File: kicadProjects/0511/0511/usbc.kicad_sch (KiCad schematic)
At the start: 13 parts, among them J1 USB4120-03-C_REVA6, U7 BD33HC5WEFJ-E2

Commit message: started to annotate and place buttons on pcb
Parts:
- renumbered CR2 to CR1, R154 to R151, R155 to R152, R156 to R153
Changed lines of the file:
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@@
 		(dnp no)
 		(fields_autoplaced yes)
-		(property "Reference" "#PWR0198"
+		(property "Reference" "#PWR0195"
 			(at 46.99 53.34 0)
 			(effects
@@
 			(project "0511"
 				(path "/2c0b0e0d-c5e7-48b7-93bb-9be1941509af/7f025c79-ea20-4013-a71e-871359ae3c80/be8e2f48-706b-43bd-b6e8-a7bcf8b61384"
-					(reference "#PWR0198")
+					(reference "#PWR0195")
 					(unit 1)
 				)
@@
 		(dnp no)
 		(fields_autoplaced yes)
-		(property "Reference" "#PWR0203"
+		(property "Reference" "#PWR0200"
 			(at 90.17 134.62 0)
 			(effects
@@
 			(project "0511"
 				(path "/2c0b0e0d-c5e7-48b7-93bb-9be1941509af/7f025c79-ea20-4013-a71e-871359ae3c80/be8e2f48-706b-43bd-b6e8-a7bcf8b61384"
-					(reference "#PWR0203")
+					(reference "#PWR0200")
 					(unit 1)
 				)
@@
 		(dnp no)
 		(fields_autoplaced yes)
-		(property "Reference" "#PWR0195"
+		(property "Reference" "#PWR0192"
 			(at 121.92 39.37 0)
 			(effects
@@
 			(project "0511"
 				(path "/2c0b0e0d-c5e7-48b7-93bb-9be1941509af/7f025c79-ea20-4013-a71e-871359ae3c80/be8e2f48-706b-43bd-b6e8-a7bcf8b61384"
-					(reference "#PWR0195")
+					(reference "#PWR0192")
 					(unit 1)
 				)
@@
 		(dnp no)
 		(fields_autoplaced yes)
-		(property "Reference" "R155"
+		(property "Reference" "R152"
 			(at 87.63 119.3799 0)
 			(effects
@@
 			(project "0511"
 				(path "/2c0b0e0d-c5e7-48b7-93bb-9be1941509af/7f025c79-ea20-4013-a71e-871359ae3c80/be8e2f48-706b-43bd-b6e8-a7bcf8b61384"
-					(reference "R155")
+					(reference "R152")
 					(unit 1)
 				)
@@
 		(dnp no)
 		(fields_autoplaced yes)
-		(property "Reference" "#PWR0200"
+		(property "Reference" "#PWR0197"
 			(at 83.82 113.03 0)
 			(effects
@@
 			(project "0511"
 				(path "/2c0b0e0d-c5e7-48b7-93bb-9be1941509af/7f025c79-ea20-4013-a71e-871359ae3c80/be8e2f48-706b-43bd-b6e8-a7bcf8b61384"
-					(reference "#PWR0200")
+					(reference "#PWR0197")
 					(unit 1)
 				)
@@
 		(dnp no)
 		(fields_autoplaced yes)
-		(property "Reference" "#PWR0197"
+		(property "Reference" "#PWR0194"
 			(at 57.15 48.26 0)
 			(effects
@@
 			(project "0511"
 				(path "/2c0b0e0d-c5e7-48b7-93bb-9be1941509af/7f025c79-ea20-4013-a71e-871359ae3c80/be8e2f48-706b-43bd-b6e8-a7bcf8b61384"
-					(reference "#PWR0197")
+					(reference "#PWR0194")
 					(unit 1)
 				)
@@
 		(dnp no)
 		(fields_autoplaced yes)
-		(property "Reference" "R156"
+		(property "Reference" "R153"
 			(at 133.35 121.9199 0)
 			(effects
@@
 			(project "0511"
 				(path "/2c0b0e0d-c5e7-48b7-93bb-9be1941509af/7f025c79-ea20-4013-a71e-871359ae3c80/be8e2f48-706b-43bd-b6e8-a7bcf8b61384"
-					(reference "R156")
+					(reference "R153")
 					(unit 1)
 				)
@@
 		(dnp no)
 		(fields_autoplaced yes)
-		(property "Reference" "#PWR0202"
+		(property "Reference" "#PWR0199"
 			(at 135.89 109.22 0)
 			(effects
@@
 			(project "0511"
 				(path "/2c0b0e0d-c5e7-48b7-93bb-9be1941509af/7f025c79-ea20-4013-a71e-871359ae3c80/be8e2f48-706b-43bd-b6e8-a7bcf8b61384"
-					(reference "#PWR0202")
+					(reference "#PWR0199")
 					(unit 1)
 				)
@@
 		(dnp no)
 		(fields_autoplaced yes)
-		(property "Reference" "R154"
+		(property "Reference" "R151"
 			(at 43.18 67.3099 0)
 			(effects
@@
 			(project "0511"
 				(path "/2c0b0e0d-c5e7-48b7-93bb-9be1941509af/7f025c79-ea20-4013-a71e-871359ae3c80/be8e2f48-706b-43bd-b6e8-a7bcf8b61384"
-					(reference "R154")
+					(reference "R151")
 					(unit 1)
 				)
@@
 		(dnp no)
 		(fields_autoplaced yes)
-		(property "Reference" "CR2"
+		(property "Reference" "CR1"
 			(at 78.74 69.85 0)
 			(effects
@@
 			(project ""
 				(path "/2c0b0e0d-c5e7-48b7-93bb-9be1941509af/7f025c79-ea20-4013-a71e-871359ae3c80/be8e2f48-706b-43bd-b6e8-a7bcf8b61384"
-					(reference "CR2")
+					(reference "CR1")
 					(unit 1)
 				)
@@
 		(dnp no)
 		(fields_autoplaced yes)
-		(property "Reference" "#PWR0199"
+		(property "Reference" "#PWR0196"
 			(at 60.96 91.44 0)
 			(effects
@@
 			(project "0511"
 				(path "/2c0b0e0d-c5e7-48b7-93bb-9be1941509af/7f025c79-ea20-4013-a71e-871359ae3c80/be8e2f48-706b-43bd-b6e8-a7bcf8b61384"
-					(reference "#PWR0199")
+					(reference "#PWR0196")
 					(unit 1)
 				)
@@
 		(dnp no)
 		(fields_autoplaced yes)
-		(property "Reference" "#PWR0201"
+		(property "Reference" "#PWR0198"
 			(at 130.81 113.03 0)
 			(effects
@@
 			(project "0511"
 				(path "/2c0b0e0d-c5e7-48b7-93bb-9be1941509af/7f025c79-ea20-4013-a71e-871359ae3c80/be8e2f48-706b-43bd-b6e8-a7bcf8b61384"
-					(reference "#PWR0201")
+					(reference "#PWR0198")
 					(unit 1)
 				)
@@
 		(dnp no)
 		(fields_autoplaced yes)
-		(property "Reference" "#PWR0196"
+		(property "Reference" "#PWR0193"
 			(at 146.05 45.72 0)
 			(effects
@@
 			(project "0511"
 				(path "/2c0b0e0d-c5e7-48b7-93bb-9be1941509af/7f025c79-ea20-4013-a71e-871359ae3c80/be8e2f48-706b-43bd-b6e8-a7bcf8b61384"
-					(reference "#PWR0196")
-					(unit 1)
-				)
+					(reference "#PWR0193")
+					(unit 1)
+				)

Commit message: poursuite placement et nommage références
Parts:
- renumbered C83 to C73, C84 to C74, C85 to C75, C86 to C76, C87 to C77, D68 to D58, D69 to D59, R151 to R131, R152 to R132, R153 to R133, U7 to U3
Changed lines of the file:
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@@
 		(dnp no)
 		(fields_autoplaced yes)
-		(property "Reference" "#PWR0195"
+		(property "Reference" "#PWR0189"
 			(at 46.99 53.34 0)
 			(effects
@@
 			(project "0511"
 				(path "/2c0b0e0d-c5e7-48b7-93bb-9be1941509af/7f025c79-ea20-4013-a71e-871359ae3c80/be8e2f48-706b-43bd-b6e8-a7bcf8b61384"
-					(reference "#PWR0195")
+					(reference "#PWR0189")
 					(unit 1)
 				)
@@
 		(on_board yes)
 		(dnp no)
-		(property "Reference" "C83"
+		(property "Reference" "C73"
 			(at 131.826 43.688 90)
 			(effects
@@
 			(project "0511"
 				(path "/2c0b0e0d-c5e7-48b7-93bb-9be1941509af/7f025c79-ea20-4013-a71e-871359ae3c80/be8e2f48-706b-43bd-b6e8-a7bcf8b61384"
-					(reference "C83")
+					(reference "C73")
 					(unit 1)
 				)
@@
 		(dnp no)
 		(fields_autoplaced yes)
-		(property "Reference" "#PWR0200"
+		(property "Reference" "#PWR0194"
 			(at 90.17 134.62 0)
 			(effects
@@
 			(project "0511"
 				(path "/2c0b0e0d-c5e7-48b7-93bb-9be1941509af/7f025c79-ea20-4013-a71e-871359ae3c80/be8e2f48-706b-43bd-b6e8-a7bcf8b61384"
-					(reference "#PWR0200")
+					(reference "#PWR0194")
 					(unit 1)
 				)
@@
 		(dnp no)
 		(fields_autoplaced yes)
-		(property "Reference" "#PWR0192"
+		(property "Reference" "#PWR0186"
 			(at 121.92 39.37 0)
 			(effects
@@
 			(project "0511"
 				(path "/2c0b0e0d-c5e7-48b7-93bb-9be1941509af/7f025c79-ea20-4013-a71e-871359ae3c80/be8e2f48-706b-43bd-b6e8-a7bcf8b61384"
-					(reference "#PWR0192")
+					(reference "#PWR0186")
 					(unit 1)
 				)
@@
 		(dnp no)
 		(fields_autoplaced yes)
-		(property "Reference" "R152"
+		(property "Reference" "R132"
 			(at 87.63 119.3799 0)
 			(effects
@@
 			(project "0511"
 				(path "/2c0b0e0d-c5e7-48b7-93bb-9be1941509af/7f025c79-ea20-4013-a71e-871359ae3c80/be8e2f48-706b-43bd-b6e8-a7bcf8b61384"
-					(reference "R152")
+					(reference "R132")
 					(unit 1)
 				)
@@
 		(dnp no)
 		(fields_autoplaced yes)
-		(property "Reference" "#PWR0197"
+		(property "Reference" "#PWR0191"
 			(at 83.82 113.03 0)
 			(effects
@@
 			(project "0511"
 				(path "/2c0b0e0d-c5e7-48b7-93bb-9be1941509af/7f025c79-ea20-4013-a71e-871359ae3c80/be8e2f48-706b-43bd-b6e8-a7bcf8b61384"
-					(reference "#PWR0197")
+					(reference "#PWR0191")
 					(unit 1)
 				)
@@
 		(dnp no)
 		(fields_autoplaced yes)
-		(property "Reference" "#PWR0194"
+		(property "Reference" "#PWR0188"
 			(at 57.15 48.26 0)
 			(effects
@@
 			(project "0511"
 				(path "/2c0b0e0d-c5e7-48b7-93bb-9be1941509af/7f025c79-ea20-4013-a71e-871359ae3c80/be8e2f48-706b-43bd-b6e8-a7bcf8b61384"
-					(reference "#PWR0194")
+					(reference "#PWR0188")
 					(unit 1)
 				)
@@
 		(dnp no)
 		(fields_autoplaced yes)
-		(property "Reference" "R153"
+		(property "Reference" "R133"
 			(at 133.35 121.9199 0)
 			(effects
@@
 			(project "0511"
 				(path "/2c0b0e0d-c5e7-48b7-93bb-9be1941509af/7f025c79-ea20-4013-a71e-871359ae3c80/be8e2f48-706b-43bd-b6e8-a7bcf8b61384"
-					(reference "R153")
+					(reference "R133")
 					(unit 1)
 				)
@@
 		(on_board yes)
 		(dnp no)
-		(property "Reference" "C84"
+		(property "Reference" "C74"
 			(at 58.42 69.088 0)
 			(effects
@@
 			(project "0511"
 				(path "/2c0b0e0d-c5e7-48b7-93bb-9be1941509af/7f025c79-ea20-4013-a71e-871359ae3c80/be8e2f48-706b-43bd-b6e8-a7bcf8b61384"
-					(reference "C84")
+					(reference "C74")
 					(unit 1)
 				)
@@
 		(dnp no)
 		(fields_autoplaced yes)
-		(property "Reference" "#PWR0199"
+		(property "Reference" "#PWR0193"
 			(at 135.89 109.22 0)
 			(effects
@@
 			(project "0511"
 				(path "/2c0b0e0d-c5e7-48b7-93bb-9be1941509af/7f025c79-ea20-4013-a71e-871359ae3c80/be8e2f48-706b-43bd-b6e8-a7bcf8b61384"
-					(reference "#PWR0199")
+					(reference "#PWR0193")
 					(unit 1)
 				)
@@
 		(dnp no)
 		(fields_autoplaced yes)
-		(property "Reference" "R151"
+		(property "Reference" "R131"
 			(at 43.18 67.3099 0)
 			(effects
@@
 			(project "0511"
 				(path "/2c0b0e0d-c5e7-48b7-93bb-9be1941509af/7f025c79-ea20-4013-a71e-871359ae3c80/be8e2f48-706b-43bd-b6e8-a7bcf8b61384"
-					(reference "R151")
+					(reference "R131")
 					(unit 1)
 				)
@@
 		(dnp no)
 		(fields_autoplaced yes)
-		(property "Reference" "#PWR0196"
+		(property "Reference" "#PWR0190"
 			(at 60.96 91.44 0)
 			(effects
@@
 			(project "0511"
 				(path "/2c0b0e0d-c5e7-48b7-93bb-9be1941509af/7f025c79-ea20-4013-a71e-871359ae3c80/be8e2f48-706b-43bd-b6e8-a7bcf8b61384"
-					(reference "#PWR0196")
+					(reference "#PWR0190")
 					(unit 1)
 				)
@@
 		(on_board yes)
 		(dnp no)
-		(property "Reference" "D68"
+		(property "Reference" "D58"
 			(at 147.32 99.9489 90)
 			(effects
@@
 			(project "0511"
 				(path "/2c0b0e0d-c5e7-48b7-93bb-9be1941509af/7f025c79-ea20-4013-a71e-871359ae3c80/be8e2f48-706b-43bd-b6e8-a7bcf8b61384"
-					(reference "D68")
+					(reference "D58")
 					(unit 1)
 				)
@@
 		(on_board yes)
 		(dnp no)
-		(property "Reference" "D69"
+		(property "Reference" "D59"
 			(at 78.74 101.2189 90)
 			(effects
@@
 			(project "0511"
 				(path "/2c0b0e0d-c5e7-48b7-93bb-9be1941509af/7f025c79-ea20-4013-a71e-871359ae3c80/be8e2f48-706b-43bd-b6e8-a7bcf8b61384"
-					(reference "D69")
+					(reference "D59")
 					(unit 1)
 				)
@@
 		(dnp no)
 		(fields_autoplaced yes)
-		(property "Reference" "U7"
+		(property "Reference" "U3"
 			(at 87.63 25.4 0)
 			(effects
@@
 			(project ""
 				(path "/2c0b0e0d-c5e7-48b7-93bb-9be1941509af/7f025c79-ea20-4013-a71e-871359ae3c80/be8e2f48-706b-43bd-b6e8-a7bcf8b61384"
-					(reference "U7")
+					(reference "U3")
 					(unit 1)
 				)
@@
 		(on_board yes)
 		(dnp no)
-		(property "Reference" "C85"
+		(property "Reference" "C75"
 			(at 74.676 88.138 90)
 			(effects
@@
 			(project "0511"
 				(path "/2c0b0e0d-c5e7-48b7-93bb-9be1941509af/7f025c79-ea20-4013-a71e-871359ae3c80/be8e2f48-706b-43bd-b6e8-a7bcf8b61384"
-					(reference "C85")
+					(reference "C75")
 					(unit 1)
 				)
@@
 		(on_board yes)
 		(dnp no)
-		(property "Reference" "C87"
+		(property "Reference" "C77"
 			(at 136.652 120.396 0)
 			(effects
@@
 			(project "0511"
 				(path "/2c0b0e0d-c5e7-48b7-93bb-9be1941509af/7f025c79-ea20-4013-a71e-871359ae3c80/be8e2f48-706b-43bd-b6e8-a7bcf8b61384"
-					(reference "C87")
+					(reference "C77")
 					(unit 1)
 				)
@@
 		(on_board yes)
 		(dnp no)
-		(property "Reference" "C86"
+		(property "Reference" "C76"
 			(at 90.932 117.856 0)
 			(effects
@@
 			(project "0511"
 				(path "/2c0b0e0d-c5e7-48b7-93bb-9be1941509af/7f025c79-ea20-4013-a71e-871359ae3c80/be8e2f48-706b-43bd-b6e8-a7bcf8b61384"
-					(reference "C86")
+					(reference "C76")
 					(unit 1)
 				)
@@
 		(dnp no)
 		(fields_autoplaced yes)
-		(property "Reference" "#PWR0198"
+		(property "Reference" "#PWR0192"
 			(at 130.81 113.03 0)
 			(effects
@@
 			(project "0511"
 				(path "/2c0b0e0d-c5e7-48b7-93bb-9be1941509af/7f025c79-ea20-4013-a71e-871359ae3c80/be8e2f48-706b-43bd-b6e8-a7bcf8b61384"
-					(reference "#PWR0198")
+					(reference "#PWR0192")
 					(unit 1)
 				)
@@
 		(dnp no)
 		(fields_autoplaced yes)
-		(property "Reference" "#PWR0193"
+		(property "Reference" "#PWR0187"
 			(at 146.05 45.72 0)
 			(effects
@@
 			(project "0511"
 				(path "/2c0b0e0d-c5e7-48b7-93bb-9be1941509af/7f025c79-ea20-4013-a71e-871359ae3c80/be8e2f48-706b-43bd-b6e8-a7bcf8b61384"
-					(reference "#PWR0193")
-					(unit 1)
-				)
+					(reference "#PWR0187")
+					(unit 1)
+				)

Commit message: poursuite routing
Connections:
- net D1+ is gone; now on net PA12: C74.2, J1.A5 (CC1), J1.B6 (D2+), R131.2
- net GND: now also D58.A, D59.A
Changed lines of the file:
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@@
+	)
+	(junction
+		(at 76.2 91.44)
+		(diameter 0)
+		(color 0 0 0 0)
+	)
+	(junction
+		(at 83.82 106.68)
+		(diameter 0)
+		(color 0 0 0 0)
 	)
 	(junction
@@
 	(wire
 		(pts
-			(xy 82.55 90.17) (xy 46.99 90.17)
+			(xy 46.99 91.44) (xy 76.2 91.44)
 		)
 		(stroke
@@
 	(wire
 		(pts
+			(xy 144.78 106.68) (xy 144.78 109.22)
+		)
+		(stroke
+			(width 0)
+			(type default)
+		)
+	)
+	(wire
+		(pts
 			(xy 107.95 38.1) (xy 111.76 38.1)
 		)
@@
 	(wire
 		(pts
+			(xy 76.2 107.95) (xy 81.28 107.95)
+		)
+		(stroke
+			(width 0)
+			(type default)
+		)
+	)
+	(wire
+		(pts
 			(xy 40.64 72.39) (xy 46.99 72.39)
 		)
@@
 	(wire
 		(pts
-			(xy 82.55 90.17) (xy 82.55 91.44)
+			(xy 81.28 106.68) (xy 83.82 106.68)
+		)
+		(stroke
+			(width 0)
+			(type default)
+		)
+	)
+	(wire
+		(pts
+			(xy 76.2 91.44) (xy 90.17 91.44)
+		)
+		(stroke
+			(width 0)
+			(type default)
+		)
+	)
+	(wire
+		(pts
+			(xy 90.17 124.46) (xy 90.17 128.27)
+		)
+		(stroke
+			(width 0)
+			(type default)
+		)
+	)
+	(wire
+		(pts
+			(xy 111.76 38.1) (xy 113.03 38.1)
+		)
+		(stroke
+			(width 0)
+			(type default)
+		)
+	)
+	(wire
+		(pts
+			(xy 81.28 83.82) (xy 83.82 83.82)
+		)
+		(stroke
+			(width 0)
+			(type default)
+		)
+	)
+	(wire
+		(pts
+			(xy 81.28 107.95) (xy 81.28 106.68)
+		)
+		(stroke
+			(width 0)
+			(type default)
+		)
+	)
+	(wire
+		(pts
+			(xy 107.95 45.72) (xy 111.76 45.72)
+		)
+		(stroke
+			(width 0)
+			(type default)
+		)
+	)
+	(wire
+		(pts
+			(xy 46.99 91.44) (xy 46.99 72.39)
+		)
+		(stroke
+			(width 0)
+			(type default)
+		)
+	)
+	(wire
+		(pts
+			(xy 46.99 72.39) (xy 52.07 72.39)
+		)
+		(stroke
+			(width 0)
+			(type default)
+		)
+	)
+	(wire
+		(pts
+			(xy 130.81 39.37) (xy 116.84 39.37)
+		)
+		(stroke
+			(width 0)
+			(type default)
+		)
+	)
+	(wire
+		(pts
+			(xy 90.17 116.84) (xy 95.25 116.84)
+		)
+		(stroke
+			(width 0)
+			(type default)
+		)
+	)
+	(wire
+		(pts
+			(xy 90.17 80.01) (xy 90.17 83.82)
+		)
+		(stroke
+			(width 0)
+			(type default)
+		)
+	)
+	(wire
+		(pts
+			(xy 60.96 83.82) (xy 60.96 85.09)
+		)
+		(stroke
+			(width 0)
+			(type default)
+		)
+	)
+	(wire
+		(pts
+			(xy 83.82 83.82) (xy 90.17 83.82)
+		)
+		(stroke
+			(width 0)
+			(type default)
+		)
+	)
+	(wire
+		(pts
+			(xy 83.82 76.2) (xy 83.82 83.82)
+		)
+		(stroke
+			(width 0)
+			(type default)
+		)
+	)
+	(wire
+		(pts
+			(xy 137.16 127) (xy 140.97 127)
+		)
+		(stroke
+			(width 0)
+			(type default)
+		)
+	)
+	(wire
+		(pts
+			(xy 46.99 64.77) (xy 52.07 64.77)
+		)
+		(stroke
+			(width 0)
+			(type default)
+		)
+	)
+	(wire
+		(pts
+			(xy 107.95 35.56) (xy 121.92 35.56)
 		)
 		(stroke
@@
 	(wire
 		(pts
-			(xy 90.17 124.46) (xy 90.17 128.27)
-		)
-		(stroke
-			(width 0)
-			(type default)
-		)
-	)
-	(wire
-		(pts
-			(xy 111.76 38.1) (xy 113.03 38.1)
-		)
-		(stroke
-			(width 0)
-			(type default)
-		)
-	)
-	(wire
-		(pts
-			(xy 81.28 83.82) (xy 83.82 83.82)
-		)
-		(stroke
-			(width 0)
-			(type default)
-		)
-	)
-	(wire
-		(pts
-			(xy 107.95 45.72) (xy 111.76 45.72)
-		)
-		(stroke
-			(width 0)
-			(type default)
-		)
-	)
-	(wire
-		(pts
-			(xy 46.99 90.17) (xy 46.99 72.39)
-		)
-		(stroke
-			(width 0)
-			(type default)
-		)
-	)
-	(wire
-		(pts
-			(xy 46.99 72.39) (xy 52.07 72.39)
-		)
-		(stroke
-			(width 0)
-			(type default)
-		)
-	)
-	(wire
-		(pts
-			(xy 130.81 39.37) (xy 116.84 39.37)
-		)
-		(stroke
-			(width 0)
-			(type default)
-		)
-	)
-	(wire
-		(pts
-			(xy 90.17 116.84) (xy 95.25 116.84)
-		)
-		(stroke
-			(width 0)
-			(type default)
-		)
-	)
-	(wire
-		(pts
-			(xy 90.17 80.01) (xy 90.17 83.82)
-		)
-		(stroke
-			(width 0)
-			(type default)
-		)
-	)
-	(wire
-		(pts
-			(xy 60.96 83.82) (xy 60.96 85.09)
-		)
-		(stroke
-			(width 0)
-			(type default)
-		)
-	)
-	(wire
-		(pts
-			(xy 83.82 83.82) (xy 90.17 83.82)
-		)
-		(stroke
-			(width 0)
-			(type default)
-		)
-	)
-	(wire
-		(pts
-			(xy 83.82 76.2) (xy 83.82 83.82)
-		)
-		(stroke
-			(width 0)
-			(type default)
-		)
-	)
-	(wire
-		(pts
-			(xy 137.16 127) (xy 140.97 127)
-		)
-		(stroke
-			(width 0)
-			(type default)
-		)
-	)
-	(wire
-		(pts
-			(xy 46.99 64.77) (xy 52.07 64.77)
-		)
-		(stroke
-			(width 0)
-			(type default)
-		)
-	)
-	(wire
-		(pts
-			(xy 90.17 91.44) (xy 82.55 91.44)
-		)
-		(stroke
-			(width 0)
-			(type default)
-		)
-	)
-	(wire
-		(pts
-			(xy 107.95 35.56) (xy 121.92 35.56)
-		)
-		(stroke
-			(width 0)
-			(type default)
-		)
-	)
-	(wire
-		(pts
 			(xy 113.03 38.1) (xy 113.03 39.37)
 		)
@@
 		(pts
 			(xy 125.73 96.52) (xy 128.27 96.52)
+		)
+		(stroke
+			(width 0)
+			(type default)
+		)
+	)
+	(wire
+		(pts
+			(xy 76.2 93.98) (xy 76.2 91.44)
 		)
 		(stroke
@@
 	)
 	(label "D1+"
-		(at 82.55 90.17 0)
+		(at 90.17 93.98 0)
 		(effects
 			(font
@@
 					(unit 1)
 				)
+			)
+		)
+	)
+	(symbol
+		(lib_id "power:GND")
+		(at 144.78 109.22 0)
+		(unit 1)
+		(exclude_from_sim no)
+		(in_bom yes)
+		(on_board yes)
+		(dnp no)
+		(fields_autoplaced yes)
+		(property "Reference" "#PWR0196"
+			(at 144.78 115.57 0)
+			(effects
+				(font
+					(size 1.27 1.27)
+				)
+				(hide yes)
+			)
+		)
+		(property "Value" "GND"
+			(at 144.78 114.3 0)
+			(effects
+				(font
+					(size 1.27 1.27)
+				)
+			)
+		)
+		(property "Footprint" ""
+			(at 144.78 109.22 0)
+			(effects
+				(font
+					(size 1.27 1.27)
+				)
+				(hide yes)
+			)
+		)
+		(property "Datasheet" ""
+			(at 144.78 109.22 0)
+			(effects
+				(font
+					(size 1.27 1.27)
+				)
+				(hide yes)
+			)
+		)
+		(property "Description" "Power symbol creates a global label with name \"GND\" , ground"
+			(at 144.78 109.22 0)
+			(effects
+				(font
+					(size 1.27 1.27)
+				)
+				(hide yes)
+			)
+		)
+		(pin "1"
+		)
+		(instances
+			(project "0511"
+				(path "/2c0b0e0d-c5e7-48b7-93bb-9be1941509af/7f025c79-ea20-4013-a71e-871359ae3c80/be8e2f48-706b-43bd-b6e8-a7bcf8b61384"
+					(reference "#PWR0196")
+					(unit 1)
+				)

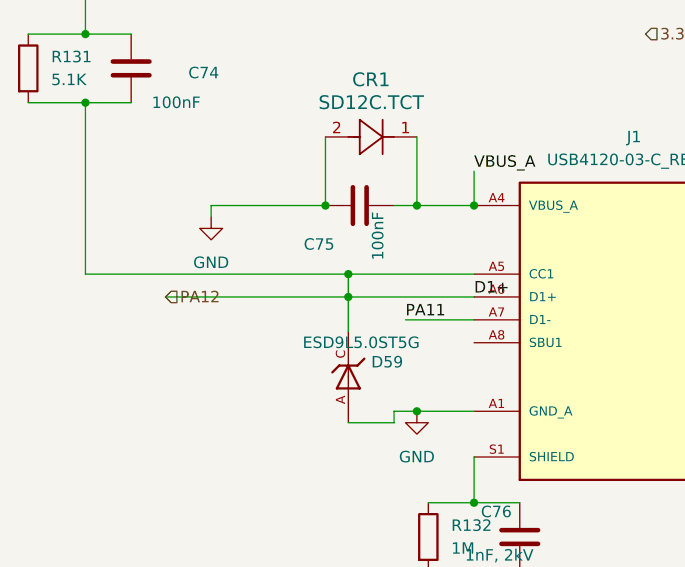
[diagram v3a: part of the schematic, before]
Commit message: poursuite placement usb c component
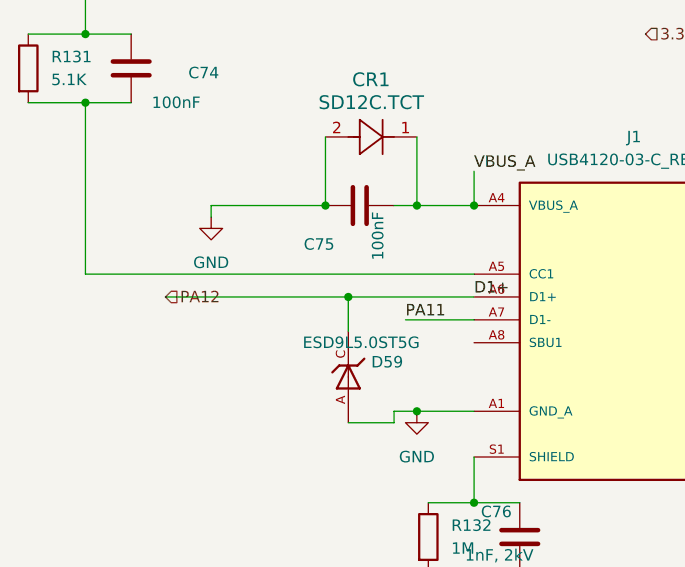
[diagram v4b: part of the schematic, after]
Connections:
- net PA12: no longer C74.2, J1.A5 (CC1), R131.2
- new net: C74.2, J1.A5 (CC1), R131.2
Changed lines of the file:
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@@
-	)
-	(junction
-		(at 76.2 91.44)
-		(diameter 0)
-		(color 0 0 0 0)
 	)
 	(junction
@@
 	(wire
 		(pts
-			(xy 46.99 91.44) (xy 76.2 91.44)
-		)
-		(stroke
-			(width 0)
-			(type default)
-		)
-	)
-	(wire
-		(pts
 			(xy 137.16 99.06) (xy 137.16 127)
 		)
@@
 	(wire
 		(pts
-			(xy 76.2 91.44) (xy 90.17 91.44)
+			(xy 46.99 91.44) (xy 90.17 91.44)
 		)
 		(stroke
@@
 		)
 		(stroke
-			(width 0)
-			(type default)
-		)
-	)
-	(wire
-		(pts
-			(xy 76.2 93.98) (xy 76.2 91.44)
-		)
-		(stroke

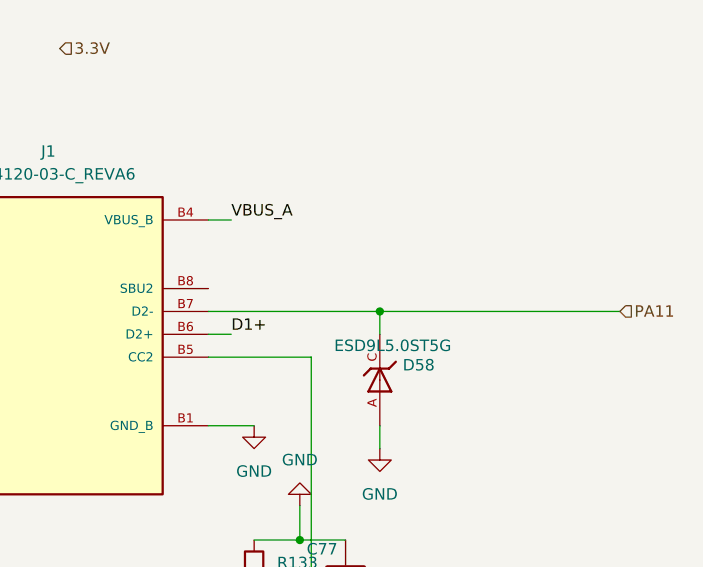
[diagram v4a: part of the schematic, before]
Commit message: added B port interruptions, updated schem and pcb
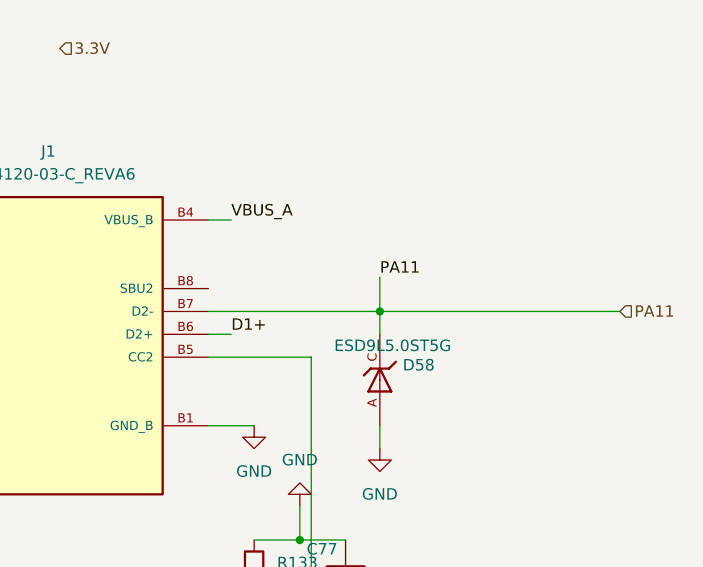
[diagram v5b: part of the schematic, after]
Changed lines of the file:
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@@
+	(wire
+		(pts
+			(xy 144.78 90.17) (xy 144.78 93.98)
+		)
+		(stroke
+			(width 0)
+			(type default)
+		)
+	)
 	(wire
 		(pts
@@
 		)
 	)
+	(label "PA11"
+		(at 144.78 90.17 0)
+		(effects
+			(font
+				(size 1.27 1.27)
+			)
+			(justify left bottom)
+		)
+	)
